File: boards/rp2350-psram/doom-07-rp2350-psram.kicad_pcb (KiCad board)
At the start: 4 copper layers, 144 x 64 mm, 86 parts, among them J2 S2B-PH-K-S(LF)(SN), J4 DM3AT-SF-PEJM5, J5 S2B-PH-K-S(LF)(SN), SW12 JS102011SAQN, U1 RP2350A, U2 W25Q128JVSIQ, U3 APS6404L-3SQR-SN, U4 TLV75533PDBVR, U5 MAX98357AETE+T, U6 BQ24074RGTR, U7 MAX17048G+T10, U8 ESD 2-line, Y1 12MHz 10pF

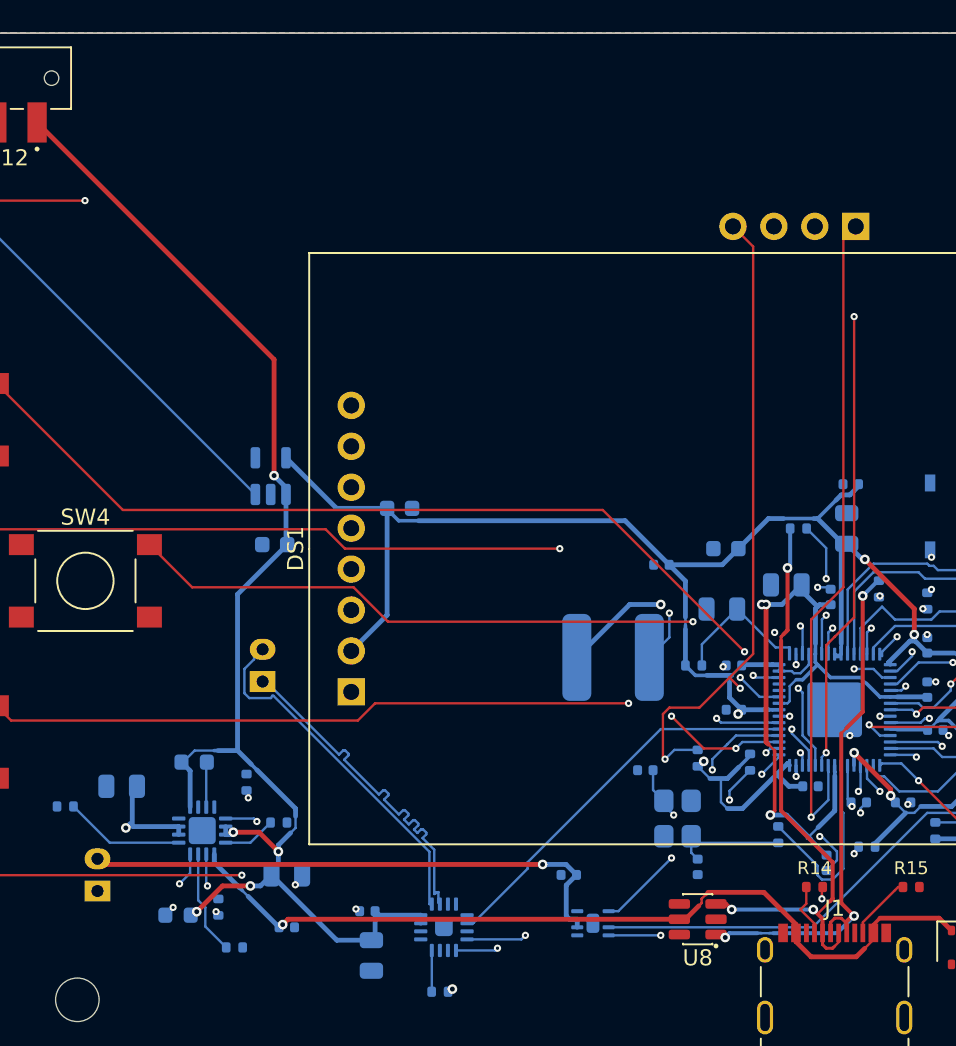
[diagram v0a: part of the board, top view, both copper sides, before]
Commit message: PCBKit's mark and pcbkit.io on every board; the RP2350 handheld ready to order
The handheld runs from two 18650 cells in parallel behind a DW01A protector and a reverse-cell
P-MOSFET, charged at up to 500 mA from the Pico's USB-C by a BQ24075 (power path into VSYS, timers
off for 6 Ah), with an on/off switch on 3V3_EN, M3 holes, ground pours and the console on pads.
Every assembled part has a JLCPCB code in stock (Basic where there is one); the module sockets are
in the BOM, the modules listed in the order's README. Check complete, the ready review clean.
Every board: routed and checked complete with the new mark.
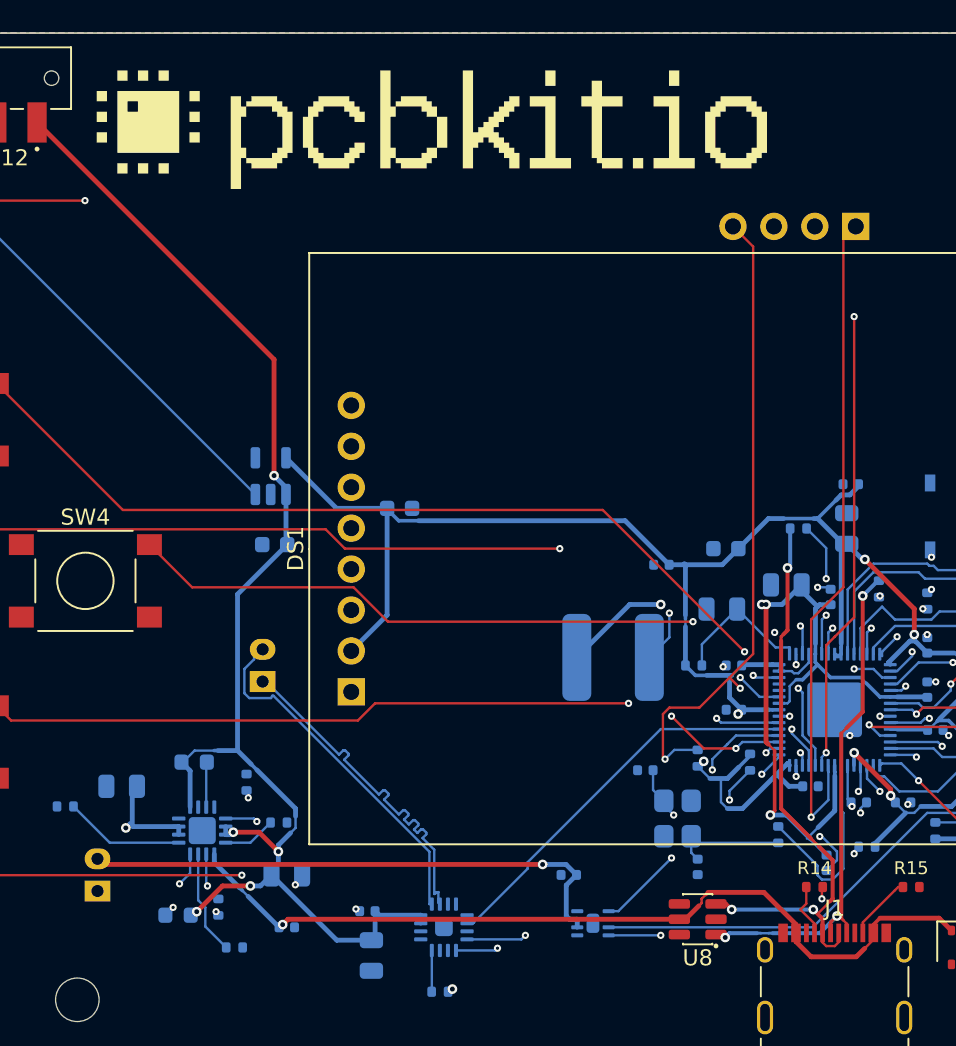
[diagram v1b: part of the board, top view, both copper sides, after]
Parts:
- added logo: , Logo_PCBKit_pcbkit.io, F.Cu at (147.0, 142.0)
- SW1, SW10, SW2, SW3, SW4, SW5, SW6, SW7, SW8, SW9: value (none) -> PTS645SM43SMTR92 LFS
- SW11: value (none) -> PTS810 SJM 250 SMTR LFS
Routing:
- net DP: track 33.9 -> 32.1 mm

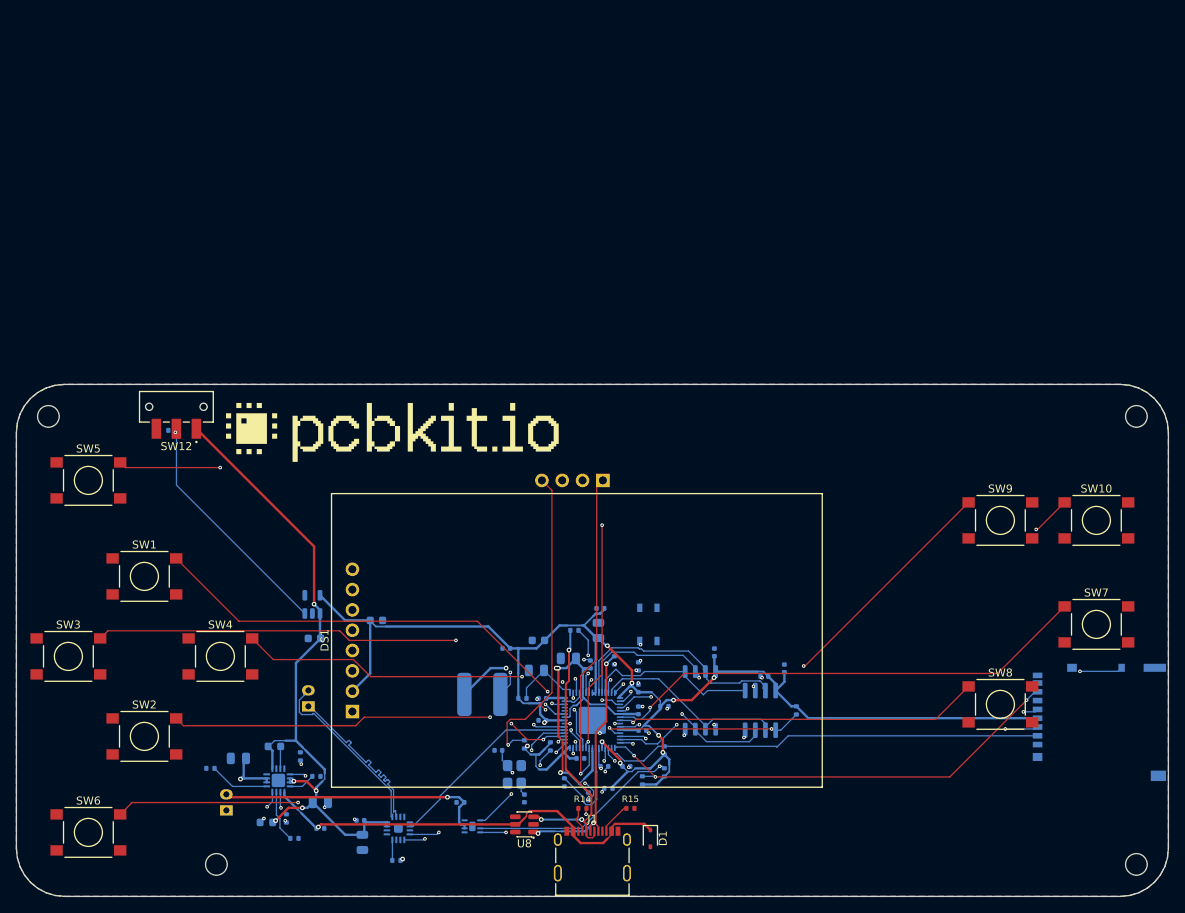
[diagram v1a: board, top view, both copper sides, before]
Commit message: rp2350-psram: two 18650 cells with protection and a BQ24075 power path; every part orderable
The LiPo and BQ24074 become two 18650 in parallel (Keystone 1042 holders on the back) behind a
reverse-cell P-FET and DW01A + FS8205A, charged by a BQ24075 in USB500 mode from the USB-C (1 A
PTC and TVS on VBUS), as rp2350-handheld; the MAX17048 gauges the pack. BOOT and RESET buttons
by the USB-C for the boot ROM's UF2 loader; In1 a solid GND plane; the RP2350's decoupling within
3 mm of each supply pin; the RP2350A part without the doubled 15 pF load capacitor on XIN; the
speaker connector on the edge; board 144 x 110 mm, M3 holes, test pads; every assembled part
pinned to an LCSC code.
check: complete, 0 errors (3 USB-pair warnings, justified); ready lens: nothing to fix; fab
export without --force.

Claude-Session: https://claude.ai/code/session_01ATmMmxyrWxFwR3nTdXUrcx
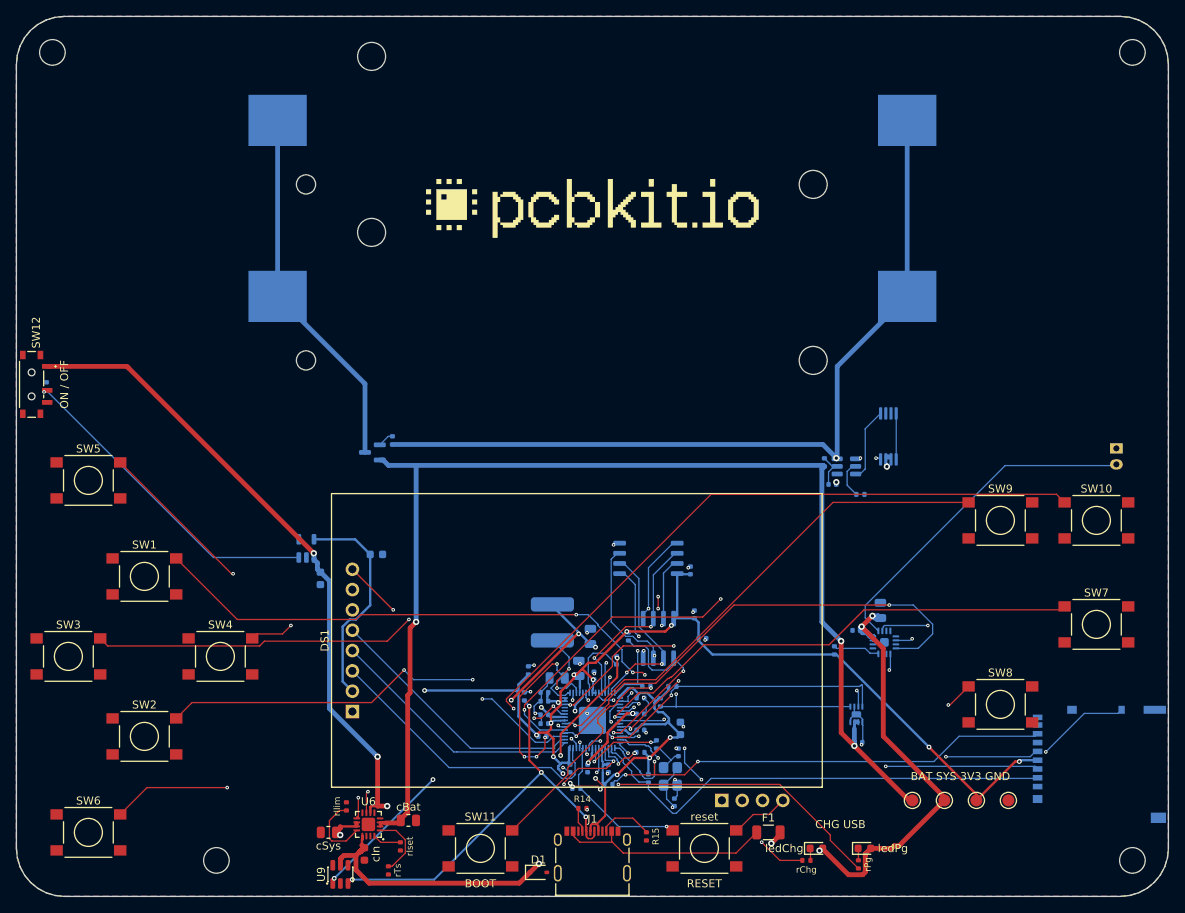
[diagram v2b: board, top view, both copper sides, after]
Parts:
- removed C24: 1uF, C_0402_1005Metric
- removed C25, C26: 4.7uF, C_0805_2012Metric
- removed D2: red, LED_0603_1608Metric
- removed D3: green, LED_0603_1608Metric
- removed J2: S2B-PH-K-S(LF)(SN), JST_PH_S2B-PH-K_1x02_P2.00mm_Horizontal
- removed R19: 46.4kohm, R_0402_1005Metric
- removed R20: 10kohm, R_0402_1005Metric
- added BT1: 1042, BatteryHolder_Keystone_1042_1x18650, B.Cu at (172.0, 125.0)
- added BT2: 1042, BatteryHolder_Keystone_1042_1x18650, B.Cu at (172.0, 103.0)
- added F1: PTC 1000mA, Fuse_1206_3216Metric, F.Cu at (194.0, 192.0)
- added Q1: AO3401A, SOT-23, B.Cu at (144.5, 144.5)
- added Q2: FS8205A, TSSOP-8_4.4x2.93mm_P0.65mm, B.Cu at (209.0, 142.5)
- added U9: ESD 2-line, SOT-23-6, F.Cu at (140.5, 197.2)
- added cBat: 4.7uF, C_0805_2012Metric, F.Cu at (149.0, 190.5)
- added cIn: 1uF, C_0603_1608Metric, F.Cu at (143.5, 194.7)
- added cSys: 4.7uF, C_0805_2012Metric, F.Cu at (139.0, 192.0)
- added ledChg: red, LED_0603_1608Metric, F.Cu at (200.0, 194.0)
- added ledPg: green, LED_0603_1608Metric, F.Cu at (206.0, 194.0)
- added rChg: 1.5kohm, R_0402_1005Metric, F.Cu at (198.8, 195.5)
- added rIlim: 1.18kohm, R_0402_1005Metric, F.Cu at (141.2, 188.8)
- added rIset: 1.13kohm, R_0402_1005Metric, F.Cu at (148.0, 193.8)
- added rPg: 1.5kohm, R_0402_1005Metric, F.Cu at (205.2, 196.0)
- added rTs: 10kohm, R_0402_1005Metric, F.Cu at (146.5, 196.8)
- added reset: PTS645SM43SMTR92 LFS, SW_Tactile_SPST_6x6mm_SMD, F.Cu at (186.0, 194.0)
- added tpBat: , TestPoint_Round_D1.5mm, F.Cu at (212.0, 188.0)
- added tpGnd: , TestPoint_Round_D1.5mm, F.Cu at (224.0, 188.0)
- added tpSys: , TestPoint_Round_D1.5mm, F.Cu at (216.0, 188.0)
- added tpV3: , TestPoint_Round_D1.5mm, F.Cu at (220.0, 188.0)
- C18: value 15pF -> 100nF
- H1, H2, H3, H4: footprint MountingHole_2.7mm_M2.5 -> MountingHole_3.2mm_M3
- R16: value 1.13kohm -> 100kohm
- R17: value 1.18kohm -> 100ohm
- R18: value 4.12kohm -> 1kohm
- SW11: value PTS810 SJM 250 SMTR LFS -> PTS645SM43SMTR92 LFS; footprint SW_Tactile_SPST_4.2x3.2mm_SMD -> SW_Tactile_SPST_6x6mm_SMD; moved to F.Cu
- SW12: value JS102011SAQN -> MSK12C02; footprint SW_Slide_SPDT_CK_JS102011SAQN_Horizontal -> SW_Slide_SPDT_Shouhan_MSK12C02
- U6: value BQ24074RGTR -> BQ24075RGTR; moved to F.Cu
- U8: value ESD 2-line -> DW01A; footprint SOT-23-6 -> SOT-6_1.6x2.9mm_P0.95mm; moved to B.Cu
- moved J5 105.4 mm to (237.5, 145.0), turned to 90 degrees
- moved R18 82.8 mm to (205.5, 149.8)
- moved R17 74.7 mm to (201.0, 145.8), turned to 90 degrees
- moved C22 70.9 mm to (208.0, 164.2), turned to 270 degrees
- moved C23 66.4 mm to (205.0, 166.8)
- moved U5 65.0 mm to (208.5, 168.2)
- moved R13 60.7 mm to (202.2, 169.2), turned to 90 degrees
- moved U8 60.2 mm to (203.8, 146.2), turned to 0 degrees
- moved C27 50.3 mm to (205.2, 180.8), turned to 180 degrees
- moved U7 50.0 mm to (205.0, 177.2), turned to 270 degrees
- moved R16 49.1 mm to (147.0, 143.0)
- moved J3 45.9 mm to (192.0, 188.0), turned to 90 degrees
- moved H3 45.5 mm to (104.5, 94.5)
- moved H4 45.5 mm to (239.5, 94.5)
- moved C18 45.3 mm to (202.0, 148.5)
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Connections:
- C18 pad 1: Net-(C2-1) -> Net-(C18-1)
- C18 pad 2: GND -> CELL_N
- C22 pad 1: VSYS -> SYS
- C23 pad 1: VSYS -> SYS
- C27 pad 1: VBAT -> BAT
- C28 pad 1: VSYS -> SYS
- J1 pad A4: VBUS -> usb/power/raw
- J1 pad B4: VBUS -> usb/power/raw
- L1 pad 1: Net-(L1-1) -> V1V1
- L1 pad 2: V1V1 -> Net-(L1-1)
- R1 pad 1: RUN -> V3
- R1 pad 2: V3 -> RUN
- R11 pad 1: QSPI_SS -> BOOTSEL
- R11 pad 2: BOOTSEL -> QSPI_SS
- R12 pad 1: PSRAM_CS -> V3
- R12 pad 2: V3 -> PSRAM_CS
- R16 pad 1: Net-(R16-1) -> CELL_N
- R16 pad 2: GND -> reversed/gate
- R17 pad 1: Net-(R17-1) -> Net-(C18-1)
- R17 pad 2: GND -> BAT
- R22 pad 1: V3 -> SCL
- R22 pad 2: SCL -> V3
- R5 pad 1: V3 -> FUEL_ALRT
- R5 pad 2: FUEL_ALRT -> V3
- R7 pad 1: Net-(R7-1) -> U1Support/XO
- R7 pad 2: U1Support/XO -> Net-(R7-1)
- R8 pad 1: Net-(C17-1) -> V3
- R8 pad 2: V3 -> Net-(C17-1)
- SW12 pad 1: VSYS -> SYS
- SW12 pad 3: GND -> (no net)
- U4 pad 1: VSYS -> SYS
- U5 pad 7: VSYS -> SYS
- U5 pad 8: VSYS -> SYS
- U6 pad 1: Net-(R20-1) -> TS
- U6 pad 10: VSYS -> SYS
- U6 pad 11: VSYS -> SYS
- U6 pad 12: Net-(R17-1) -> ILIM
- U6 pad 14: Net-(R19-1) -> GND
- U6 pad 15: Net-(R18-1) -> GND
- U6 pad 16: Net-(R16-1) -> ISET
- U6 pad 2: VBAT -> BAT
- U6 pad 3: VBAT -> BAT
- U6 pad 5: VSYS -> GND
- U6 pad 6: GND -> SYS
- U6 pad 7: Net-(D3-1) -> PG_N
- U6 pad 9: Net-(D2-1) -> CHG_N
- U7 pad 2: VBAT -> BAT
- U7 pad 3: VBAT -> BAT
- U8 pad 1: DP -> Net-(Q2-4)
- U8 pad 2: GND -> Net-(R18-1)
- U8 pad 3: DN -> Net-(Q2-5)
- U8 pad 5: VBUS -> Net-(C18-1)
- U8 pad 6: (no net) -> CELL_N
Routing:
- net SYS: track 0.00 -> 211.8 mm, vias 0 -> 7
- net BAT: track 0.00 -> 155.6 mm, vias 0 -> 3
- net CELL_N: track 0.00 -> 112.0 mm, vias 0 -> 3
- net VSYS: track 85.1 -> 0.00 mm, vias 5 -> 0
- net PG_N: track 0.00 -> 69.1 mm, vias 0 -> 2
- net CHG_N: track 0.00 -> 62.0 mm, vias 0 -> 2
- net BAT_IN: track 0.00 -> 46.0 mm
- net VBAT: track 43.2 -> 0.00 mm, vias 2 -> 0
- net I2S_LRCK: track 24.6 -> 65.2 mm, vias 0 -> 3
- net I2S_BCK: track 25.0 -> 60.9 mm
- net SCL: track 35.1 -> 70.7 mm, vias 2 -> 4
- net DP: track 32.1 -> 64.5 mm, vias 3 -> 5
- net usb/power/raw: track 0.00 -> 26.9 mm
- net FUEL_ALRT: track 22.7 -> 49.0 mm
- net BOOTSEL: track 2.00 -> 27.2 mm, vias 2 -> 1
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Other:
- board size 144 x 64 mm -> 144 x 110 mm
- board text added: "+"
- board text added: "-"
- board text added: "2 x 18650 Li-ion 3.7 V"
- board text added: "BAT SYS 3V3 GND"
- board text added: "BOOT"
- board text added: "CHG USB"
- board text added: "ON / OFF"
- board text added: "RESET"
